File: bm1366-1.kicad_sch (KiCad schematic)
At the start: 54 parts, among them U1 25MHz, U10 AP7331, U11 AP7331, U14 BM1366_mode1

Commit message: minor update
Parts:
- removed U14: BM1366_mode1, bitaxe:BM1366, symbol bitaxe:BM1366_mode1
- added U27, U28: BM1368_mode1, bitaxe:BM1368, symbol bitaxe:BM1368_mode1
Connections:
- net 0V8: now also U27.13 (PLL_VSS), U27.18 (VSS)
- net 1V8: now also U27.14 (VDDIO_08_0), U27.17 (VDDIO_08_1)
- net BI1: now also U27.6 (CI)
- net CI: now also U27.9 (BI)
- net CLKI1: now also U27.8 (CLKI)
- net GND1: now also U27.12 (INV_CLKO), U27.19 (PIN_MODE), U27.27 (VSS), U27.32 (VSS), U27.4 (VSS)
- net NRSTI: now also U27.5 (NRSTI)
- net RO: now also U27.7 (RO)
- net VDD1: now also U27.31 (VDD)
- net at C2.2, C3.1: now also U27.3 (VDD1_0)
- net at C15.2, C17.1, C3.2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: now also U27.29 (VDD2_1)
- net at C12.2, C15.1, C6.2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: now also U27.30 (VDD3_1)
- net at C6.2, C8.1: now also U27.1 (VDD3_0)
- net at TP13.1: now also U27.10 (ROSC_SEL)
- net at TP13.1: now also U27.11 (LITE_PAD)
- net at TP13.1: now also U27.21 (TEMP_N)
- net at C3.2, C6.1: now also U27.2 (VDD2_0)
- net at U14.9 (CI): now also U27.22 (BO)
- net at U14.8 (CLKI): now also U27.23 (CLKO)
- net at U14.7 (RO): now also U27.24 (RI)
- net at U14.6 (BI): now also U27.25 (CO)
- net at R6.2, U14.5 (NRSTI): now also U27.26 (NRSTO)
- net at C17.2, C18.1, C2.2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: now also U27.28 (VDD1_1)
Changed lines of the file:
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@@
 	)
 	(junction
+		(at 72.39 115.57)
+		(diameter 0)
+		(color 0 0 0 0)
+	)
+	(junction
 		(at 74.93 161.29)
 		(diameter 0)
@@
 	(wire
 		(pts
+			(xy 72.39 115.57) (xy 72.39 127)
+		)
+		(stroke
+			(width 0)
+			(type default)
+		)
+	)
+	(wire
+		(pts
 			(xy 156.21 102.87) (xy 156.21 127)
 		)
@@
 	(wire
 		(pts
-			(xy 72.39 113.03) (xy 72.39 127)
+			(xy 72.39 113.03) (xy 72.39 115.57)
 		)
 		(stroke
@@
 	)
 	(symbol
-		(lib_name "BM1366_mode1_1")
-		(lib_id "bitaxe:BM1366_mode1")
-		(at 72.39 92.71 0)
-		(unit 1)
-		(exclude_from_sim no)
-		(in_bom yes)
-		(on_board yes)
-		(dnp no)
-		(property "Reference" "U14"
-			(at 57.15 71.12 0)
-			(effects
-				(font
-					(size 1.27 1.27)
-				)
-				(justify left)
-			)
-		)
-		(property "Value" "BM1366_mode1"
-			(at 74.93 71.12 0)
-			(effects
-				(font
-					(size 1.27 1.27)
-				)
-				(justify left)
-			)
-		)
-		(property "Footprint" "bitaxe:BM1366"
-			(at 64.77 92.71 0)
-			(effects
-				(font
-					(size 1.27 1.27)
-				)
-				(hide yes)
-			)
-		)
-		(property "Datasheet" ""
-			(at 64.77 92.71 0)
-			(effects
-				(font
-					(size 1.27 1.27)
-				)
-				(hide yes)
-			)
-		)
-		(property "Description" ""
-			(at 72.39 92.71 0)
-			(effects
-				(font
-					(size 1.27 1.27)
-				)
-				(hide yes)
-			)
-		)
-		(pin "1"
-		)
-		(pin "10"
-		)
-		(pin "11"
-		)
-		(pin "12"
-		)
-		(pin "13"
-		)
-		(pin "14"
-		)
-		(pin "15"
-		)
-		(pin "16"
-		)
-		(pin "17"
-		)
-		(pin "18"
-		)
-		(pin "19"
-		)
-		(pin "2"
-		)
-		(pin "20"
-		)
-		(pin "21"
-		)
-		(pin "22"
-		)
-		(pin "23"
-		)
-		(pin "24"
-		)
-		(pin "25"
-		)
-		(pin "26"
-		)
-		(pin "27"
-		)
-		(pin "28"
-		)
-		(pin "29"
-		)
-		(pin "3"
-		)
-		(pin "30"
-		)
-		(pin "4"
-		)
-		(pin "5"
-		)
-		(pin "6"
-		)
-		(pin "7"
-		)
-		(pin "8"
-		)
-		(pin "9"
-		)
-		(instances
-			(project "bm1366"
-				(path "/5ffa02c9-1f90-4b06-abee-1fc0c47a0c88"
-					(reference "U14")
-					(unit 1)
-				)
-			)
-			(project "bitaxeHex"
-				(path "/e63e39d7-6ac0-4ffd-8aa3-1841a4541b55/4cf9c075-d009-4c35-9949-adda70ae20c7"
-					(reference "U12")
-					(unit 1)
-				)
-			)
-		)
-	)
-	(symbol
 		(lib_id "Device:C")
 		(at 55.88 66.04 90)
@@
 	)
 	(symbol
+		(lib_id "bitaxe:BM1368_mode1")
+		(at 199.39 35.56 0)
+		(unit 1)
+		(exclude_from_sim no)
+		(in_bom yes)
+		(on_board yes)
+		(dnp no)
+		(fields_autoplaced yes)
+		(property "Reference" "U28"
+			(at 201.5841 10.16 0)
+			(effects
+				(font
+					(size 1.27 1.27)
+				)
+				(justify left)
+			)
+		)
+		(property "Value" "BM1368_mode1"
+			(at 201.5841 12.7 0)
+			(effects
+				(font
+					(size 1.27 1.27)
+				)
+				(justify left)
+			)
+		)
+		(property "Footprint" "bitaxe:BM1368"
+			(at 215.9 68.58 0)
+			(effects
+				(font
+					(size 1.27 1.27)
+				)
+				(hide yes)
+			)
+		)
+		(property "Datasheet" ""
+			(at 191.77 35.56 0)
+			(effects
+				(font
+					(size 1.27 1.27)
+				)
+				(hide yes)
+			)
+		)
+		(property "Description" ""
+			(at 199.39 35.56 0)
+			(effects
+				(font
+					(size 1.27 1.27)
+				)
+				(hide yes)
+			)
+		)
+		(pin "8"
+		)
+		(pin "12"
+		)
+		(pin "10"
+		)
+		(pin "26"
+		)
+		(pin "6"
+		)
+		(pin "11"
+		)
+		(pin "18"
+		)
+		(pin "27"
+		)
+		(pin "4"
+		)
+		(pin "25"
+		)
+		(pin "1"
+		)
+		(pin "16"
+		)
+		(pin "28"
+		)
+		(pin "30"
+		)
+		(pin "21"
+		)
+		(pin "14"
+		)
+		(pin "23"
+		)
+		(pin "15"
+		)
+		(pin "2"
+		)
+		(pin "13"
+		)
+		(pin "20"
+		)
+		(pin "17"
+		)
+		(pin "24"
+		)
+		(pin "9"
+		)
+		(pin "7"
+		)
+		(pin "29"
+		)
+		(pin "31"
+		)
+		(pin "19"
+		)
+		(pin "22"
+		)
+		(pin "32"
+		)
+		(pin "5"
+		)
+		(pin "3"
+		)
+		(instances
+			(project "bitaxeHex"
+				(path "/e63e39d7-6ac0-4ffd-8aa3-1841a4541b55/4cf9c075-d009-4c35-9949-adda70ae20c7"
+					(reference "U28")
+					(unit 1)
+				)
+			)
+		)
+	)
+	(symbol
 		(lib_id "Device:C")
 		(at 41.91 118.11 0)
@@
 					(unit 1)
 				)
+			)
+		)
+	)
+	(symbol
+		(lib_id "bitaxe:BM1368_mode1")
+		(at 72.39 92.71 0)
+		(unit 1)
+		(exclude_from_sim no)
+		(in_bom yes)
+		(on_board yes)
+		(dnp no)
+		(fields_autoplaced yes)
+		(property "Reference" "U27"
+			(at 74.5841 67.31 0)
+			(effects
+				(font
+					(size 1.27 1.27)
+				)
+				(justify left)
+			)
+		)
+		(property "Value" "BM1368_mode1"
+			(at 74.5841 69.85 0)
+			(effects
+				(font
+					(size 1.27 1.27)
+				)
+				(justify left)
+			)
+		)
+		(property "Footprint" "bitaxe:BM1368"
+			(at 88.9 125.73 0)
+			(effects
+				(font
+					(size 1.27 1.27)
+				)
+				(hide yes)
+			)
+		)
+		(property "Datasheet" ""
+			(at 64.77 92.71 0)
+			(effects
+				(font
+					(size 1.27 1.27)
+				)
+				(hide yes)
+			)
+		)
+		(property "Description" ""
+			(at 72.39 92.71 0)
+			(effects
+				(font
+					(size 1.27 1.27)
+				)
+				(hide yes)
+			)
+		)
+		(pin "5"
+		)
+		(pin "23"
+		)
+		(pin "13"
+		)
+		(pin "25"
+		)
+		(pin "12"
+		)
+		(pin "3"
+		)
+		(pin "1"
+		)
+		(pin "14"
+		)
+		(pin "27"
+		)
+		(pin "29"
+		)
+		(pin "18"
+		)
+		(pin "10"
+		)
+		(pin "26"
+		)
+		(pin "20"
+		)
+		(pin "11"
+		)
+		(pin "8"
+		)
+		(pin "9"
+		)
+		(pin "15"
+		)
+		(pin "7"
+		)
+		(pin "31"
+		)
+		(pin "30"
+		)
+		(pin "16"
+		)
+		(pin "2"
+		)
+		(pin "32"
+		)
+		(pin "21"
+		)
+		(pin "28"
+		)
+		(pin "17"
+		)
+		(pin "22"
+		)
+		(pin "19"
+		)
+		(pin "4"
+		)
+		(pin "6"
+		)
+		(pin "24"
+		)
+		(instances
+			(project "bitaxeHex"
+				(path "/e63e39d7-6ac0-4ffd-8aa3-1841a4541b55/4cf9c075-d009-4c35-9949-adda70ae20c7"
+					(reference "U27")
+					(unit 1)
+				)

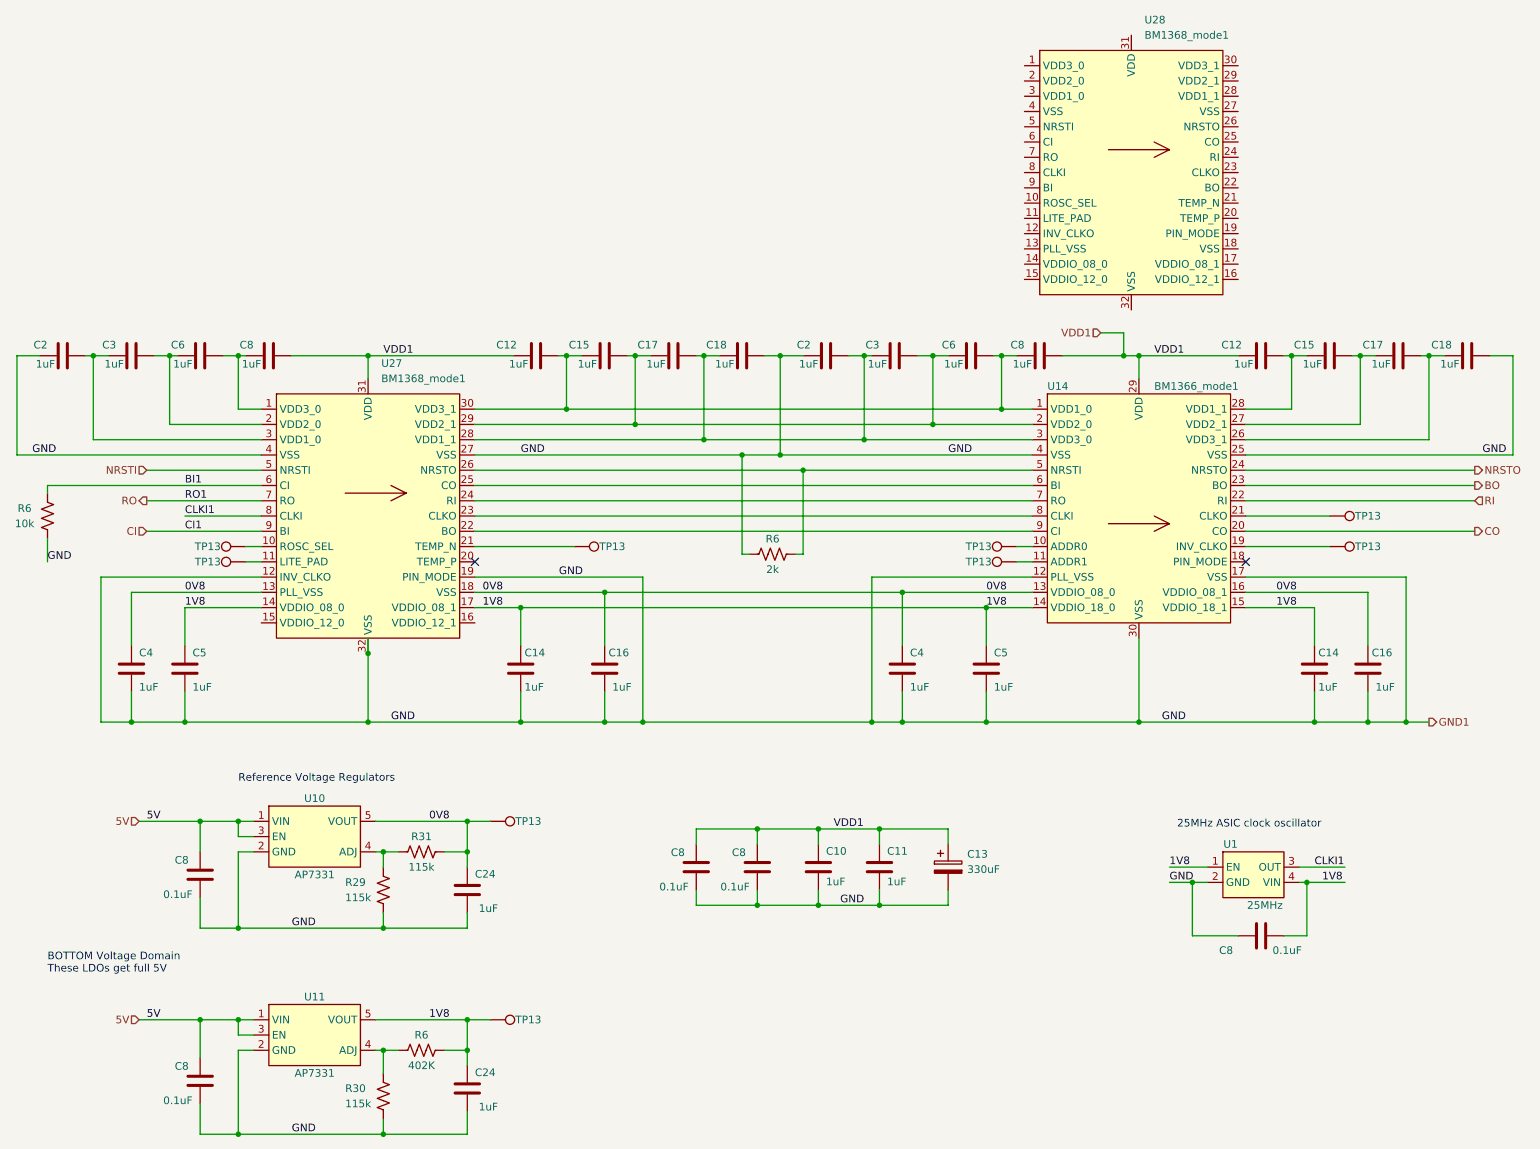
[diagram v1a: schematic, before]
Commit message: finish sch rearrange for BM1368 chain
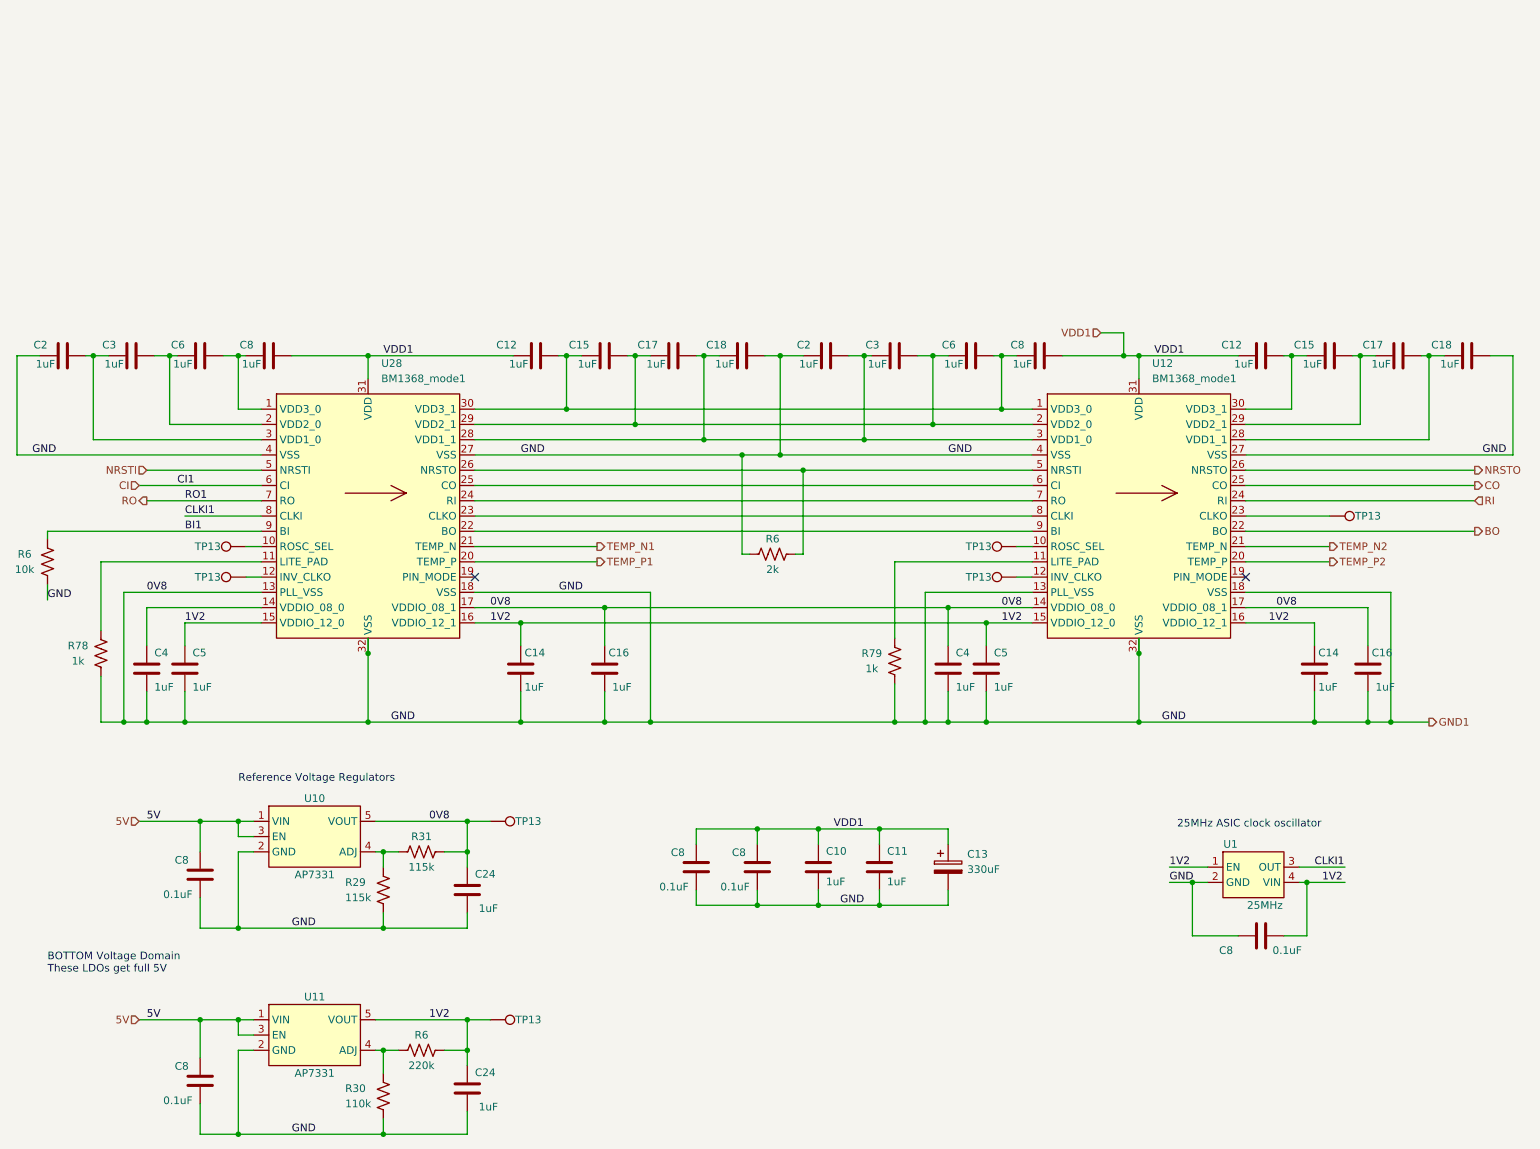
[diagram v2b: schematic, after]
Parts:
- removed TP13 (x2): TestPoint, TestPoint:TestPoint_Pad_D1.0mm, symbol Connector:TestPoint
- removed U14: BM1366_mode1, bitaxe:BM1366, symbol bitaxe:BM1366_mode1
- removed U27: BM1368_mode1, bitaxe:BM1368, symbol bitaxe:BM1368_mode1
- added R78, R79: 1k, Resistor_SMD:R_0402_1005Metric, symbol Device:R_US
- added U12: BM1368_mode1, bitaxe:BM1368, symbol bitaxe:BM1368_mode1
- R30: value 115k -> 110k; DK YAG2956CT-ND -> 311-110KLRTR-ND; PARTNO RC0402FR-07115KL -> RC0402FR-07110KL
- R6: value 402K -> 220k; DK YAG3151CT-ND -> 311-220KLRTR-ND; PARTNO RC0402FR-07402KL -> RC0402FR-07220KL
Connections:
- net 1V8 is gone; now on net 1V2: C14.1, C14.1, C24.1, C5.1, C5.1, C8.1, R6.1, TP13.1, U1.1 (EN), U1.4 (VIN), U11.5 (VOUT)
- net BI1: now also U28.9 (BI)
- net BO: now also U12.22 (BO)
- net CI: now also U28.6 (CI)
- net CLKI1: now also U28.8 (CLKI)
- net CO: now also U12.25 (CO)
- net GND1: now also C16.1, C16.1, C24.1, C4.1, R31.2, TP13.1, U10.5 (VOUT), U28.13 (PLL_VSS), U28.17 (VDDIO_08_1), U28.18 (VSS), U28.27 (VSS), U28.32 (VSS), U28.4 (VSS), R78.1, R79.1, U12.13 (PLL_VSS), U12.14 (VDDIO_08_0), U12.17 (VDDIO_08_1), U12.18 (VSS), U12.27 (VSS), U12.32 (VSS), U12.4 (VSS)
- net NRSTI: now also U28.5 (NRSTI)
- net NRSTO: now also U12.26 (NRSTO)
- net RI: now also U12.24 (RI)
- net RO: now also U28.7 (RO)
- net VDD1: now also U28.31 (VDD), U12.31 (VDD)
- net at C2.2, C3.1: now also U28.3 (VDD1_0)
- net at C15.2, C17.1, C3.2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: now also U28.29 (VDD2_1), U12.2 (VDD2_0)
- net at C12.2, C15.1, C6.2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: now also U28.30 (VDD3_1), U12.1 (VDD3_0)
- net at C6.2, C8.1: now also U28.1 (VDD3_0)
- net at R6.2: now also U28.26 (NRSTO), U12.5 (NRSTI)
- net at C15.2, C17.1: now also U12.29 (VDD2_1)
- net at C17.2, C18.1: now also U12.28 (VDD1_1)
- net at C3.2, C6.1: now also U28.2 (VDD2_0)
- net at C17.2, C18.1, C2.2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: now also U28.28 (VDD1_1), U12.3 (VDD1_0)
- net at U28.10 (ROSC_SEL): now also TP13.1
- net at U28.11 (LITE_PAD): now also R78.2
- net at U28.12 (INV_CLKO): now also TP13.1
- net at U28.14 (VDDIO_08_0): now also C4.1
- net 1V2: now reaches U28.15 (VDDIO_12_0)
- net 1V2: now also U28.16 (VDDIO_12_1), U12.15 (VDDIO_12_0), U12.16 (VDDIO_12_1)
- net TEMP_P1: now reaches U28.20 (TEMP_P)
- net TEMP_N1: now reaches U28.21 (TEMP_N)
- net at U28.22 (BO): now also U12.9 (BI)
- net at U28.23 (CLKO): now also U12.8 (CLKI)
- net at U28.24 (RI): now also U12.7 (RO)
- net at U28.25 (CO): now also U12.6 (CI)
- net at TP13.1: now also U12.12 (INV_CLKO)
- net at TP13.1: now also U12.10 (ROSC_SEL)
- net at TP13.1: now also U12.23 (CLKO)
- net at C12.2, C15.1: now also U12.30 (VDD3_1)
- removed net 0V8: C16.1, C16.1, C24.1, C4.1, C4.1, R31.2, TP13.1, U10.5 (VOUT)
- new net: R79.2, U12.11 (LITE_PAD)
- new net TEMP_N2: U12.21 (TEMP_N)
- new net TEMP_P2: U12.20 (TEMP_P)
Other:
- moved on the sheet: C4, R6, TP13, U28

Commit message: Reset to 1V8
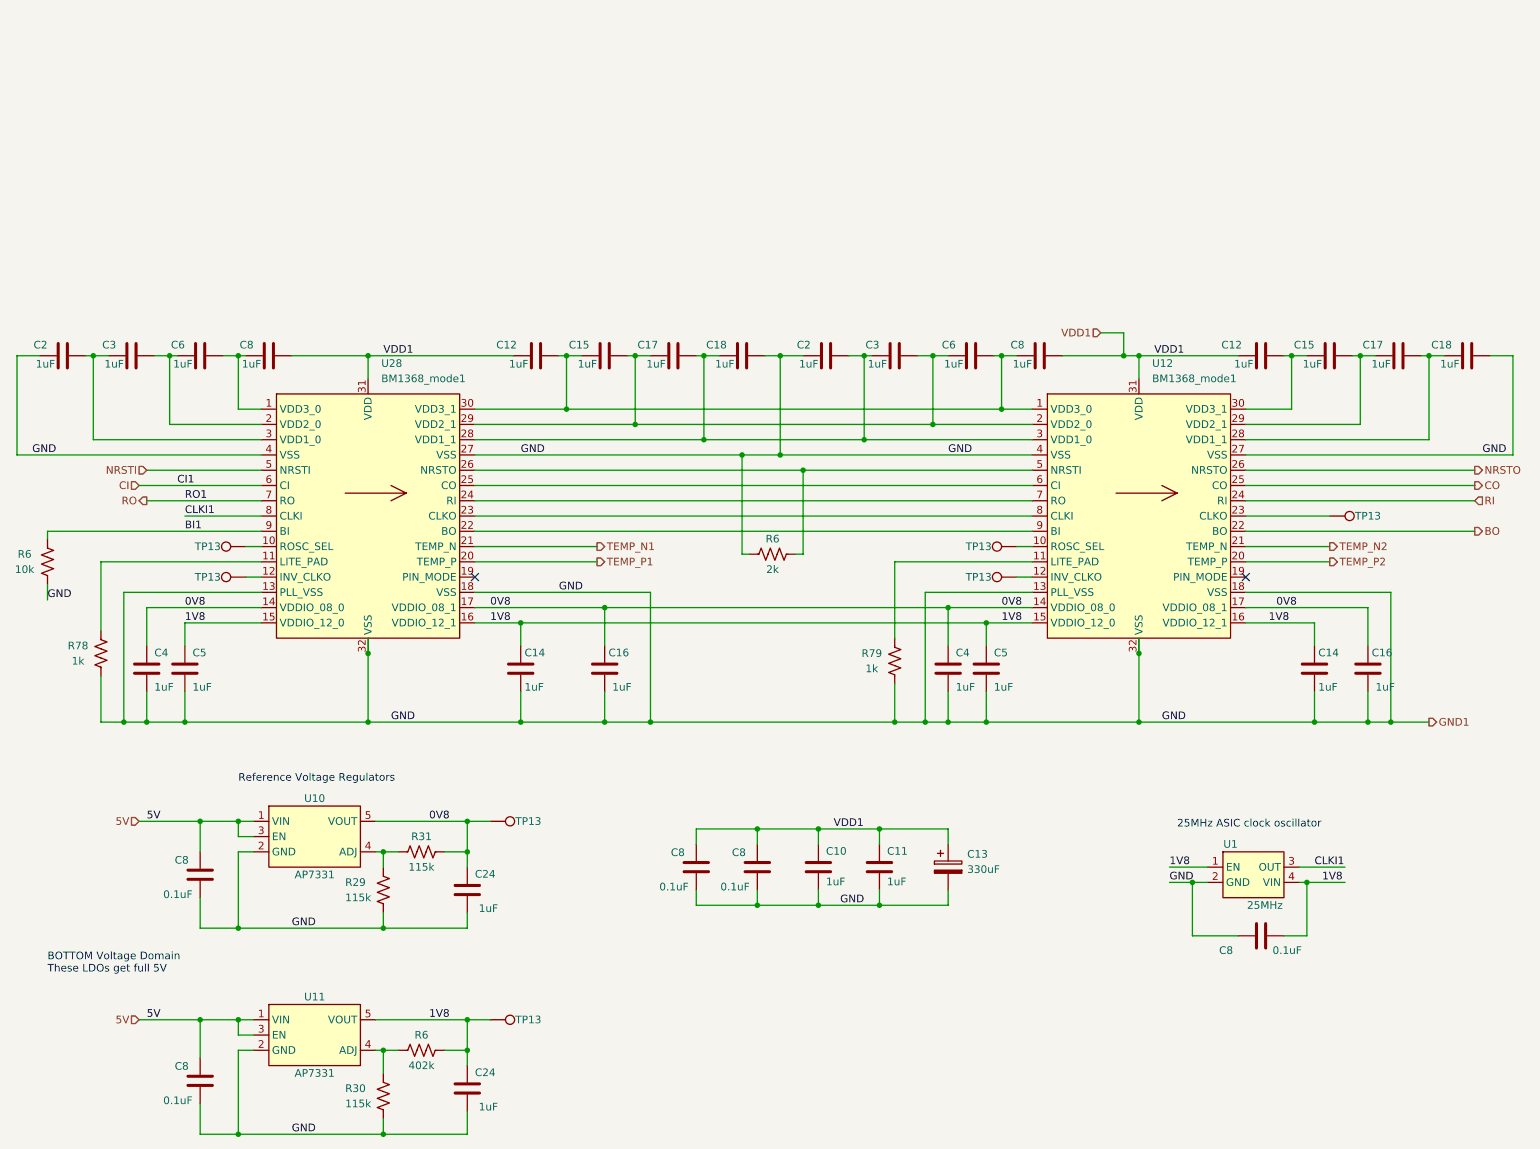
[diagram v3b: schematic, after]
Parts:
- R30: value 110k -> 115k; DK 311-110KLRTR-ND -> YAG2956CT-ND; PARTNO RC0402FR-07110KL -> RC0402FR-07115KL
- R6: value 220k -> 402k; DK 311-220KLRTR-ND -> YAG3151CT-ND; PARTNO RC0402FR-07220KL -> RC0402FR-07402KL
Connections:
- net GND1: no longer C16.1, C16.1, C24.1, C4.1, R31.2, TP13.1, U10.5 (VOUT), U12.14 (VDDIO_08_0), U12.17 (VDDIO_08_1), U28.17 (VDDIO_08_1)
- net 0V8: now reaches C4.1, U28.14 (VDDIO_08_0)
- net 0V8: now also C16.1, C16.1, C24.1, C4.1, R31.2, TP13.1, U10.5 (VOUT), U12.14 (VDDIO_08_0), U12.17 (VDDIO_08_1), U28.17 (VDDIO_08_1)
- net 1V2 renamed 1V8
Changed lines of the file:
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@@
 		)
 	)
-	(label "0V8"
-		(at 35.56 105.41 0)
-		(fields_autoplaced yes)
-		(effects
-			(font
-				(size 1.27 1.27)
-			)
-			(justify left bottom)
-		)
-	)
 	(label "GND"
 		(at 19.05 106.68 0)
@@
 		)
 	)
-	(label "1V2"
+	(label "1V8"
 		(at 205.74 151.13 0)
 		(fields_autoplaced yes)
@@
 		)
 	)
-	(label "1V2"
+	(label "1V8"
 		(at 92.71 110.49 0)
 		(fields_autoplaced yes)
@@
 		)
 	)
-	(label "1V2"
+	(label "1V8"
 		(at 231.14 153.67 0)
 		(fields_autoplaced yes)
@@
 		)
 	)
-	(label "1V2"
+	(label "1V8"
 		(at 82.55 176.53 0)
 		(fields_autoplaced yes)
@@
 		)
 	)
-	(label "1V2"
+	(label "1V8"
 		(at 41.91 110.49 0)
 		(fields_autoplaced yes)
@@
 		)
 	)
-	(label "1V2"
+	(label "1V8"
 		(at 177.8 110.49 0)
 		(fields_autoplaced yes)
@@
 		)
 	)
+	(label "0V8"
+		(at 41.91 107.95 0)
+		(fields_autoplaced yes)
+		(effects
+			(font
+				(size 1.27 1.27)
+			)
+			(justify left bottom)
+		)
+	)
 	(label "GND"
 		(at 76.2 127 0)
@@
 		)
 	)
-	(label "1V2"
+	(label "1V8"
 		(at 222.25 110.49 0)
 		(fields_autoplaced yes)
@@
 			)
 		)
-		(property "Value" "220k"
+		(property "Value" "402k"
 			(at 81.28 184.15 90)
 			(effects
@@
 			)
 		)
-		(property "DK" "311-220KLRTR-ND"
+		(property "DK" "YAG3151CT-ND"
 			(at 81.28 181.61 0)
 			(effects
@@
 			)
 		)
-		(property "PARTNO" "RC0402FR-07220KL"
+		(property "PARTNO" "RC0402FR-07402KL"
 			(at 81.28 181.61 0)
 			(effects
@@
 			)
 		)
-		(property "Value" "110k"
+		(property "Value" "115k"
 			(at 68.58 190.5 0)
 			(effects
@@
 			)
 		)
-		(property "DK" "311-110KLRTR-ND"
+		(property "DK" "YAG2956CT-ND"
 			(at 74.93 189.23 0)
 			(effects
@@
 			)
 		)
-		(property "PARTNO" "RC0402FR-07110KL"
+		(property "PARTNO" "RC0402FR-07115KL"
 			(at 74.93 189.23 0)
 			(effects
